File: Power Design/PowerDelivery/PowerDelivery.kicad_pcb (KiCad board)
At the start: 2 copper layers, 85.1 x 85.1 mm, 29 parts, among them J1 Conn_01x06_Pin, J2 Conn_01x24_Socket, J3 Screw_Terminal_01x08, Q1 Q_NPN_CBE, U1 Opamp_Dual, U2 Opamp_Dual, U3 2EDN8524FXTMA1, U4 IPP016N06NF2SAKMA1, U5 Opamp_Dual

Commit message: moved connectors and added mounting holes
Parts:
- moved J1 32.5 mm to (150.3, 130.2), turned to 0 degrees
- moved J2 13.0 mm to (186.2, 121.6)
- moved J3 2.31 mm to (136.7, 59.8)
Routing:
- net +3.3V: track 61.9 -> 88.3 mm
- net voltage_sense_out: track 72.6 -> 92.3 mm
- net current_sense_out: track 65.2 -> 83.7 mm
- net fault_signal: track 53.6 -> 68.6 mm
- net mc_trigger: track 57.9 -> 47.2 mm
- net +12V: track 243.9 -> 253.2 mm
- net -12V: track 75.8 -> 83.8 mm
- net load: track 70.8 -> 68.7 mm
- net GND: vias 23 -> 27
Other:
- board size 85.1 x 85.1 mm -> 85 x 85 mm

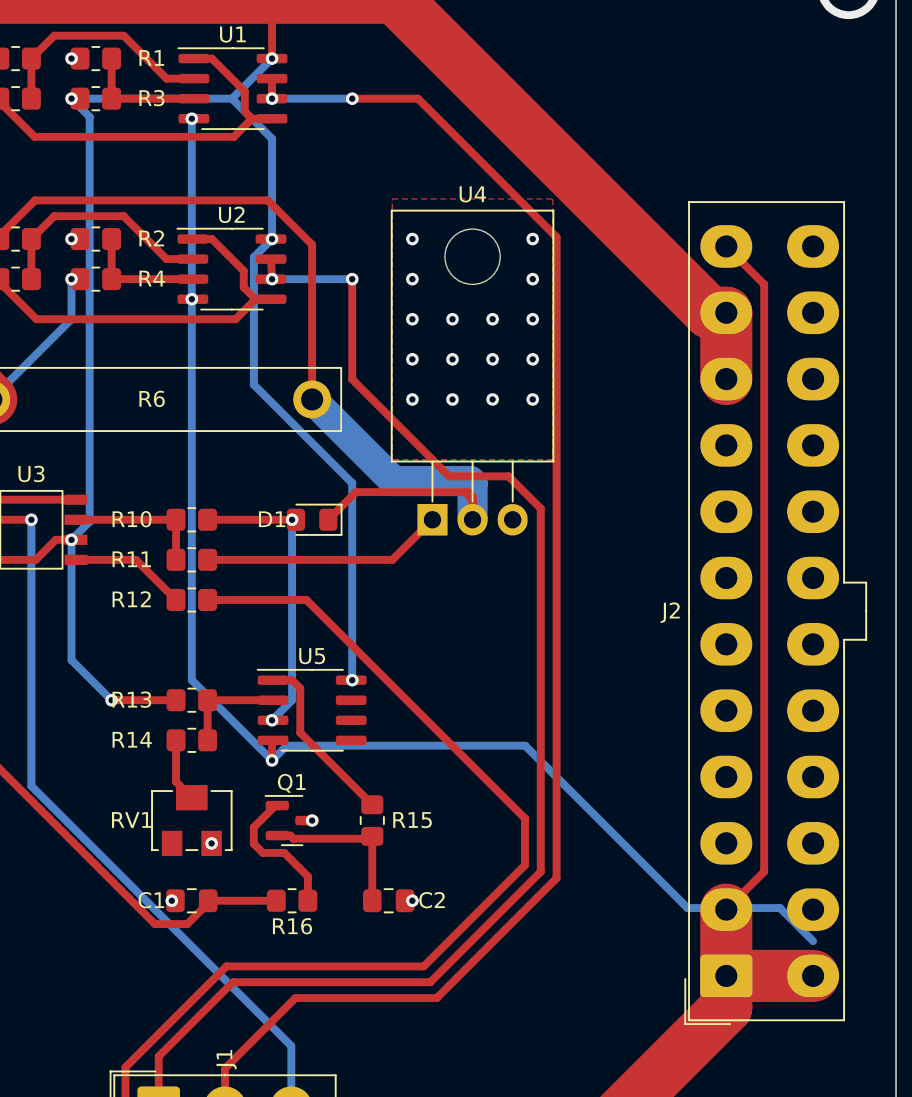
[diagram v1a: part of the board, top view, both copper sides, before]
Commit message: moved connectors and added mounting holes
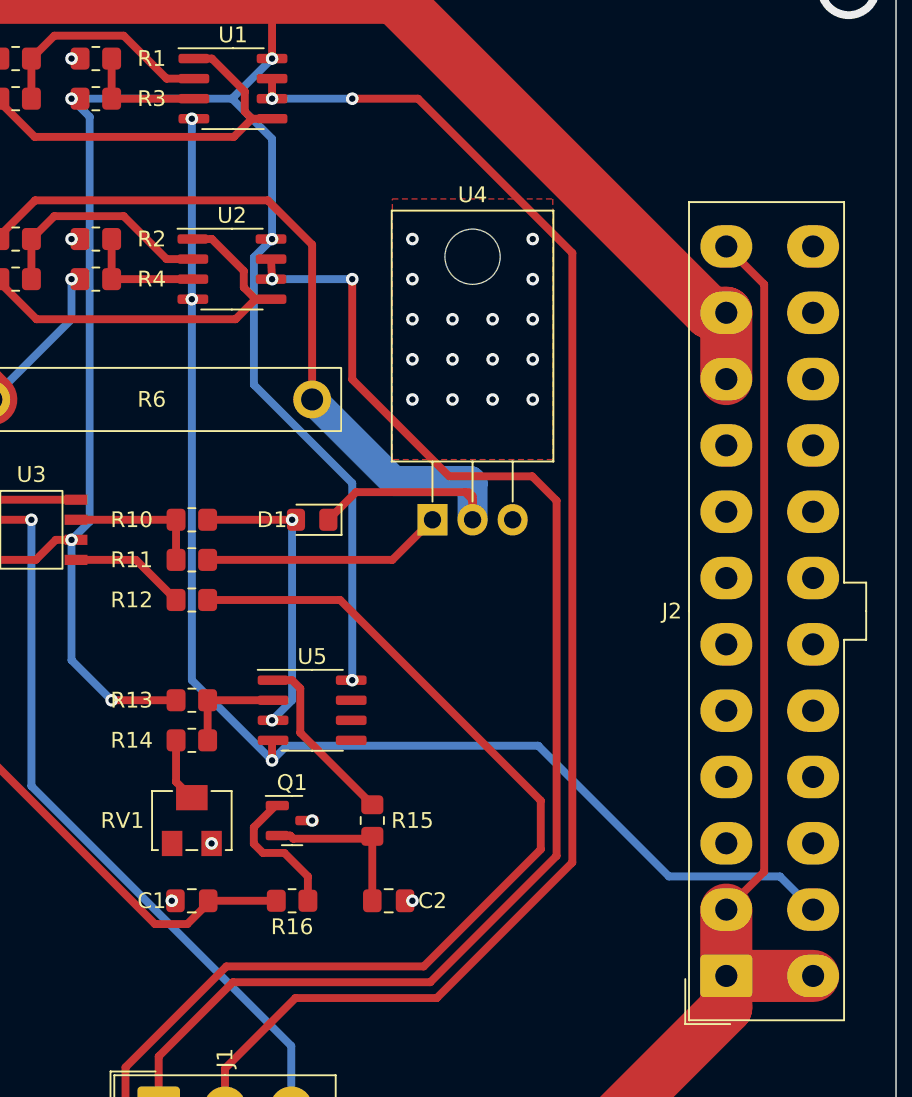
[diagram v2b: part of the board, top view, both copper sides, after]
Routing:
- net fault_signal: track 68.6 -> 70.7 mm
- net current_sense_out: track 83.7 -> 85.4 mm
- net -12V: track 83.8 -> 83.0 mm
- net voltage_sense_out: track 92.3 -> 93.1 mm
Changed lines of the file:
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@@
     (property "ki_keywords" "resistor variable")
     (attr smd)
-    (fp_text reference "RV1" (at 3.81 0) (layer "F.SilkS")
+    (fp_text reference "RV1" (at 4.4 0) (layer "F.SilkS")
         (effects (font (size 1 1) (thickness 0.15)))
     )
@@
   (segment (start 158.75 104.14) (end 157.48 105.41) (width 0.5) (layer "B.Cu") (net 4))
   (segment (start 158.75 92.71) (end 158.75 104.14) (width 0.5) (layer "B.Cu") (net 4))
+  (segment (start 175.5 91.5) (end 175.5 114) (width 0.5) (layer "F.Cu") (net 5))
+  (segment (start 168.7 89.96) (end 173.96 89.96) (width 0.5) (layer "F.Cu") (net 5))
+  (segment (start 162.56 77.47) (end 162.56 83.82) (width 0.5) (layer "F.Cu") (net 5))
+  (segment (start 173.96 89.96) (end 175.5 91.5) (width 0.5) (layer "F.Cu") (net 5))
+  (segment (start 157.415 76.2) (end 157.48 77.47) (width 0.5) (layer "F.Cu") (net 5))
+  (segment (start 175.5 114) (end 167.5 122) (width 0.5) (layer "F.Cu") (net 5))
+  (segment (start 155 122) (end 150.3 126.7) (width 0.5) (layer "F.Cu") (net 5))
+  (segment (start 162.56 83.82) (end 168.7 89.96) (width 0.5) (layer "F.Cu") (net 5))
+  (segment (start 157.48 77.47) (end 157.415 77.47) (width 0.5) (layer "F.Cu") (net 5))
+  (segment (start 167.5 122) (end 155 122) (width 0.5) (layer "F.Cu") (net 5))
   (segment (start 150.3 126.7) (end 150.3 130.25) (width 0.5) (layer "F.Cu") (net 5))
-  (segment (start 162.56 77.47) (end 162.56 83.82) (width 0.5) (layer "F.Cu") (net 5))
-  (segment (start 162.56 83.82) (end 168.7 89.96) (width 0.5) (layer "F.Cu") (net 5))
-  (segment (start 155 122) (end 150.3 126.7) (width 0.5) (layer "F.Cu") (net 5))
-  (segment (start 157.415 76.2) (end 157.48 77.47) (width 0.5) (layer "F.Cu") (net 5))
-  (segment (start 172.459999 89.959999) (end 174.5 92) (width 0.5) (layer "F.Cu") (net 5))
-  (segment (start 167.5 122) (end 155 122) (width 0.5) (layer "F.Cu") (net 5))
-  (segment (start 174.5 92) (end 174.5 115) (width 0.5) (layer "F.Cu") (net 5))
-  (segment (start 168.7 89.96) (end 172.459999 89.959999) (width 0.5) (layer "F.Cu") (net 5))
-  (segment (start 174.5 115) (end 167.5 122) (width 0.5) (layer "F.Cu") (net 5))
-  (segment (start 157.48 77.47) (end 157.415 77.47) (width 0.5) (layer "F.Cu") (net 5))
   (via (at 157.48 77.47) (size 0.8) (drill 0.4) (layers "F.Cu" "B.Cu") (net 5))
   (via (at 162.56 77.47) (size 0.8) (drill 0.4) (layers "F.Cu" "B.Cu") (free) (net 5))
   (segment (start 157.48 77.47) (end 162.56 77.47) (width 0.5) (layer "B.Cu") (net 5))
-  (segment (start 175.500001 115.414213) (end 175.5 74.813654) (width 0.5) (layer "F.Cu") (net 6))
-  (segment (start 175.5 74.813654) (end 166.726346 66.04) (width 0.5) (layer "F.Cu") (net 6))
-  (segment (start 154.5 130.25) (end 154.5 127.464214) (width 0.5) (layer "F.Cu") (net 6))
-  (segment (start 167.914214 123) (end 175.500001 115.414213) (width 0.5) (layer "F.Cu") (net 6))
+  (segment (start 176.5 75.813654) (end 166.726346 66.04) (width 0.5) (layer "F.Cu") (net 6))
+  (segment (start 154.5 127.464214) (end 158.964214 123) (width 0.5) (layer "F.Cu") (net 6))
+  (segment (start 176.5 114.414214) (end 176.5 75.813654) (width 0.5) (layer "F.Cu") (net 6))
+  (segment (start 166.726346 66.04) (end 162.56 66.04) (width 0.5) (layer "F.Cu") (net 6))
   (segment (start 157.48 66.04) (end 157.48 64.77) (width 0.5) (layer "F.Cu") (net 6))
   (segment (start 158.964214 123) (end 167.914214 123) (width 0.5) (layer "F.Cu") (net 6))
-  (segment (start 166.726346 66.04) (end 162.56 66.04) (width 0.5) (layer "F.Cu") (net 6))
-  (segment (start 154.5 127.464214) (end 158.964214 123) (width 0.5) (layer "F.Cu") (net 6))
+  (segment (start 167.914214 123) (end 176.5 114.414214) (width 0.5) (layer "F.Cu") (net 6))
+  (segment (start 154.5 130.25) (end 154.5 127.464214) (width 0.5) (layer "F.Cu") (net 6))
   (via (at 157.48 66.04) (size 0.8) (drill 0.4) (layers "F.Cu" "B.Cu") (net 6))
   (via (at 162.56 66.04) (size 0.8) (drill 0.4) (layers "F.Cu" "B.Cu") (free) (net 6))
@@
   (segment (start 158.7 126.036346) (end 158.7 130.25) (width 0.5) (layer "B.Cu") (net 7))
   (segment (start 142.24 109.576346) (end 158.7 126.036346) (width 0.5) (layer "B.Cu") (net 7))
+  (segment (start 174.5 113.585786) (end 167.085786 121) (width 0.5) (layer "F.Cu") (net 8))
+  (segment (start 148.2 133.65) (end 150.3 135.75) (width 0.5) (layer "F.Cu") (net 8))
   (segment (start 148.2 127.385786) (end 148.2 133.65) (width 0.5) (layer "F.Cu") (net 8))
+  (segment (start 161.79 97.79) (end 174.5 110.5) (width 0.5) (layer "F.Cu") (net 8))
   (segment (start 154.585786 121) (end 148.2 127.385786) (width 0.5) (layer "F.Cu") (net 8))
-  (segment (start 153.4 97.79) (end 159.662792 97.79) (width 0.5) (layer "F.Cu") (net 8))
-  (segment (start 173.5 114.585786) (end 167.085786 121) (width 0.5) (layer "F.Cu") (net 8))
-  (segment (start 148.2 133.65) (end 150.3 135.75) (width 0.5) (layer "F.Cu") (net 8))
-  (segment (start 173.5 111.627208) (end 173.5 114.585786) (width 0.5) (layer "F.Cu") (net 8))
+  (segment (start 153.4 97.79) (end 161.79 97.79) (width 0.5) (layer "F.Cu") (net 8))
   (segment (start 167.085786 121) (end 154.585786 121) (width 0.5) (layer "F.Cu") (net 8))
-  (segment (start 159.662792 97.79) (end 173.5 111.627208) (width 0.5) (layer "F.Cu") (net 8))
+  (segment (start 174.5 110.5) (end 174.5 113.585786) (width 0.5) (layer "F.Cu") (net 8))
   (segment (start 158.7 135.75) (end 174.1 135.75) (width 3.3) (layer "F.Cu") (net 9))
   (segment (start 186.25 121.6) (end 186.25 123.6) (width 3.3) (layer "F.Cu") (net 9))
@@
   (via (at 157.48 107.95) (size 0.8) (drill 0.4) (layers "F.Cu" "B.Cu") (free) (net 15))
   (via (at 152.4 67.31) (size 0.8) (drill 0.4) (layers "F.Cu" "B.Cu") (net 15))
+  (segment (start 158.41 107.02) (end 174.339848 107.02) (width 0.5) (layer "B.Cu") (net 15))
   (segment (start 152.4 67.31) (end 152.4 78.74) (width 0.5) (layer "B.Cu") (net 15))
-  (segment (start 183.794214 117.3) (end 189.65 117.3) (width 0.5) (layer "B.Cu") (net 15))
-  (segment (start 158.41 107.02) (end 173.514214 107.02) (width 0.5) (layer "B.Cu") (net 15))
+  (segment (start 189.65 115.3) (end 191.75 117.4) (width 0.5) (layer "B.Cu") (net 15))
+  (segment (start 157.48 107.95) (end 158.41 107.02) (width 0.5) (layer "B.Cu") (net 15))
   (segment (start 157.48 107.95) (end 152.4 102.87) (width 0.5) (layer "B.Cu") (net 15))
   (segment (start 152.4 102.87) (end 152.4 78.74) (width 0.5) (layer "B.Cu") (net 15))
-  (segment (start 173.514214 107.02) (end 183.794214 117.3) (width 0.5) (layer "B.Cu") (net 15))
-  (segment (start 157.48 107.95) (end 158.41 107.02) (width 0.5) (layer "B.Cu") (net 15))
-  (segment (start 189.65 117.3) (end 191.75 119.4) (width 0.5) (layer "B.Cu") (net 15))
+  (segment (start 174.339848 107.02) (end 182.619848 115.3) (width 0.5) (layer "B.Cu") (net 15))
+  (segment (start 182.619848 115.3) (end 189.65 115.3) (width 0.5) (layer "B.Cu") (net 15))
   (segment (start 138.5 83.89) (end 138.5 65.24) (width 0.5) (layer "F.Cu") (net 21))
   (segment (start 139.7 85.09) (end 138.5 83.89) (width 0.5) (layer "F.Cu") (net 21))
@@
   (zone (net 2) (net_name "GND") (layers "F&B.Cu") (hatch edge 0.5)
     (connect_pads (clearance 0.5))
-    (min_thickness 0.26) (filled_areas_thickness no)
+    (min_thickness 0.27) (filled_areas_thickness no)
     (fill yes (thermal_gap 0.5) (thermal_bridge_width 1))
     (polygon
